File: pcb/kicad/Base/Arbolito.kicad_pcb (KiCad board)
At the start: 2 copper layers, 73 x 66 mm, 61 parts, among them J1 Battery, J2 Conn_01x06_Female, P1 USB_C_Plug_USB2.0, Q1 S8050, Q2 S8050, Q3 S8050, SW1 SW_DP3T, SW2 SW_Push, SW3 SW_Push, SW4 SW_Push, U1 NCP115AMX120TCG, U2 CH340C, U3 AP63205WU, U4 ESP-12F, U5 SHT31-DIS

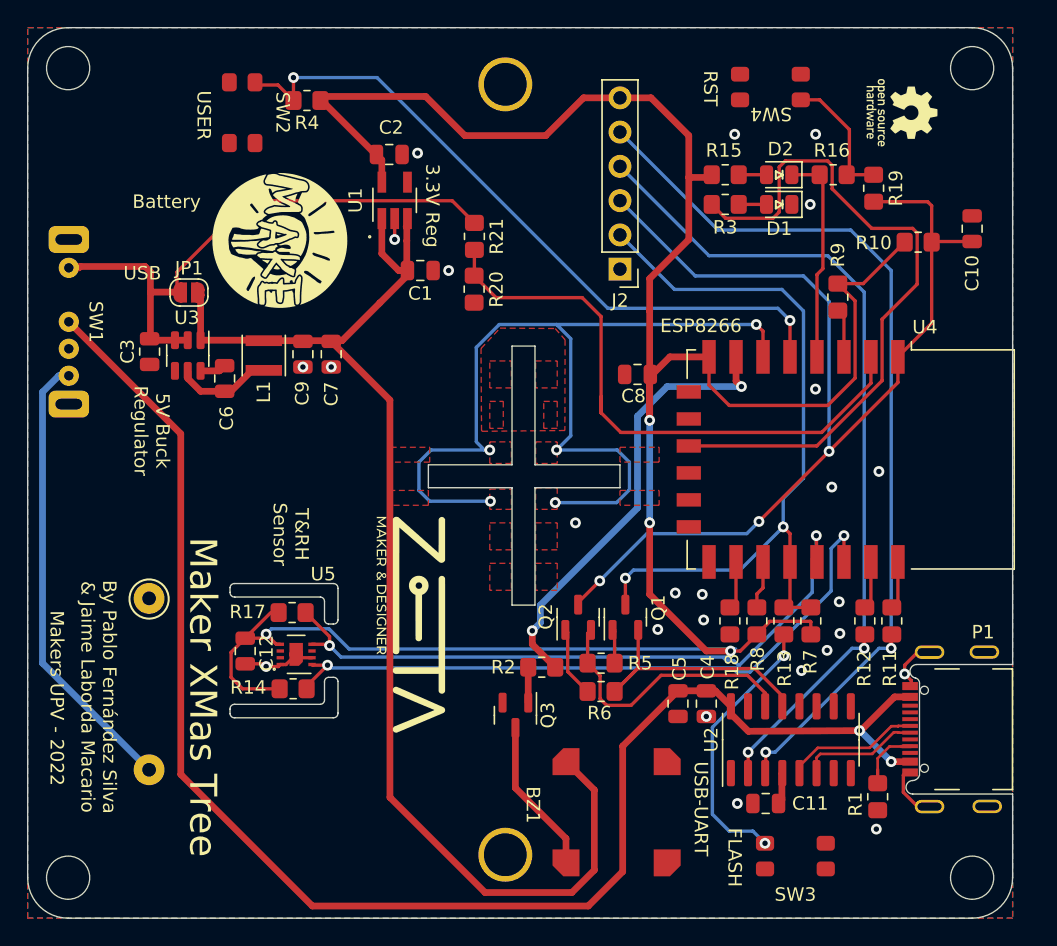
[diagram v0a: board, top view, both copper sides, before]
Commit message: Footprints corrected
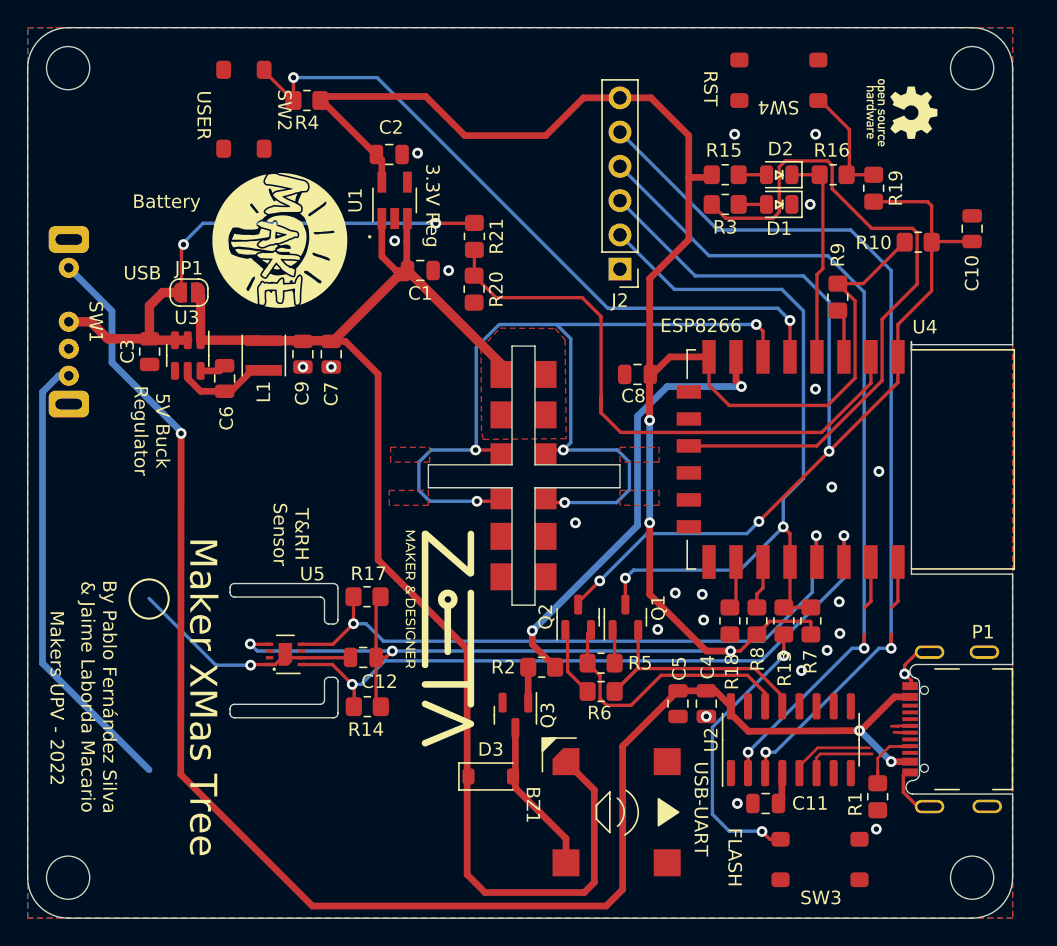
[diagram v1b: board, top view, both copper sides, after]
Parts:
- removed J1: Battery, Library:Battery
- removed R11, R12: 330, Resistor_SMD:R_0805_2012Metric_Pad1.20x1.40mm_HandSolder
- added D3: SD103AW, Diode_SMD:D_SOD-123, F.Cu at (139.3, 117.5)
- added J10: Conn_01x01, Library:Pad_tree_PS, F.Cu at (140.1, 87.7)
- added J11: Conn_01x01, Library:Pad_tree_PS, F.Cu at (140.1, 99.7)
- added J12: Conn_01x01, Library:Pad_tree_PS, F.Cu at (143.4, 102.7)
- added J13: Conn_01x01, Library:Pad_tree_PS, F.Cu at (140.1, 102.7)
- added J14: Conn_01x01, Library:Pad_tree_PS, F.Cu at (143.4, 99.7)
- added J3: Conn_01x01, Library:Pad_tree_Data, F.Cu at (140.1, 93.6)
- added J4: Conn_01x01, Library:Pad_tree_Data, F.Cu at (143.4, 93.6)
- added J5: Conn_01x01, Library:Pad_tree_Data, F.Cu at (143.4, 96.9)
- added J6: Conn_01x01, Library:Pad_tree_Data, F.Cu at (140.1, 96.9)
- added J7: Conn_01x01, Library:Pad_tree_PS, F.Cu at (143.4, 87.7)
- added J8: Conn_01x01, Library:Pad_tree_PS, F.Cu at (140.1, 90.7)
- added J9: Conn_01x01, Library:Pad_tree_PS, F.Cu at (143.4, 90.7)
- moved C12 8.76 mm to (129.9, 108.7), turned to 180 degrees
- moved R17 5.67 mm to (130.2, 104.2), turned to 0 degrees
- moved R14 5.66 mm to (130.2, 112.3), turned to 0 degrees
- moved G*** 2.38 mm to (135.6, 107.3)
- moved SW3 1.92 mm to (163.8, 123.7)
- moved U5 0.80 mm to (124.1, 108.5)
- moved SW4 0.74 mm to (160.6, 65.9)
- moved SW2 0.22 mm to (121.0, 68.1)
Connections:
- net /Boton renamed /BUTTON
- SW1 pad 1: VCC -> VBUS
- SW1 pad 2: VBUS -> VCC
- U4 pad 21: Net-(U4-GPIO3/RXD) -> /TX
- U4 pad 22: Net-(U4-GPIO1/TXD) -> /RX
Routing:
- net +5V: track 91.9 -> 103.7 mm
- net GND: track 13.6 -> 24.0 mm
- net VBUS: track 114.6 -> 119.4 mm, vias 2 -> 3
- net /TX: track 62.8 -> 66.3 mm
- net /RX: track 67.5 -> 71.0 mm
- net Net-(U4-GPIO3/RXD): track 3.56 -> 0.00 mm
- net Net-(U4-GPIO1/TXD): track 3.56 -> 0.00 mm
- net /DIN: track 69.5 -> 72.3 mm
- net /D+: track 8.87 -> 6.61 mm
- net /D-: track 9.44 -> 7.17 mm
- net VCC: track 42.9 -> 40.7 mm, vias 0 -> 2
- net +3.3V: track 176.3 -> 174.8 mm, vias 4 -> 5
- net Net-(R16-Pad1): track 9.94 -> 8.54 mm
- net Net-(R13-Pad1): track 20.5 -> 21.5 mm
- net /SCL: track 49.9 -> 49.0 mm
- removed copper zone on F.Cu, net /DIN
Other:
- outline, holes or cut-outs redrawn

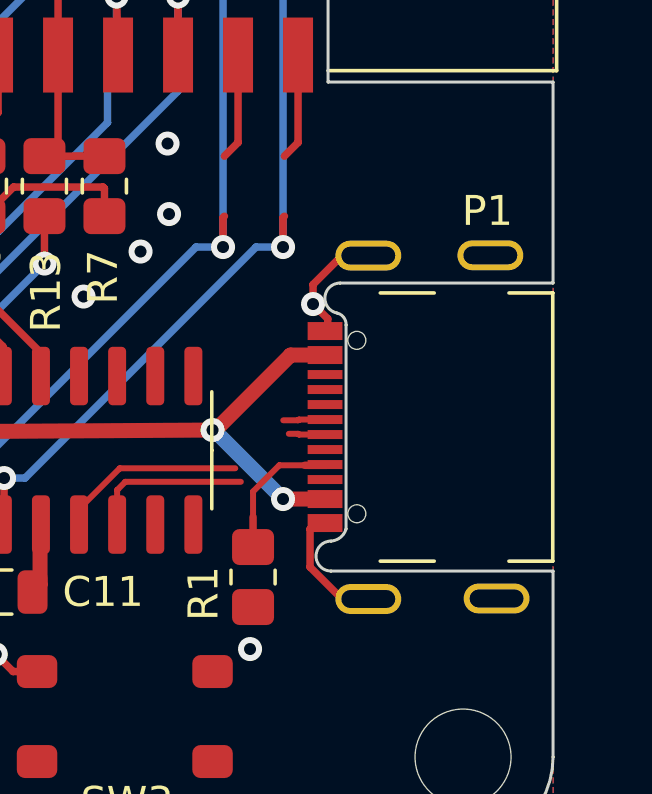
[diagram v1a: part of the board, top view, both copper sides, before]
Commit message: Modified USB C Molex 2169900002 footprint and added 3D step
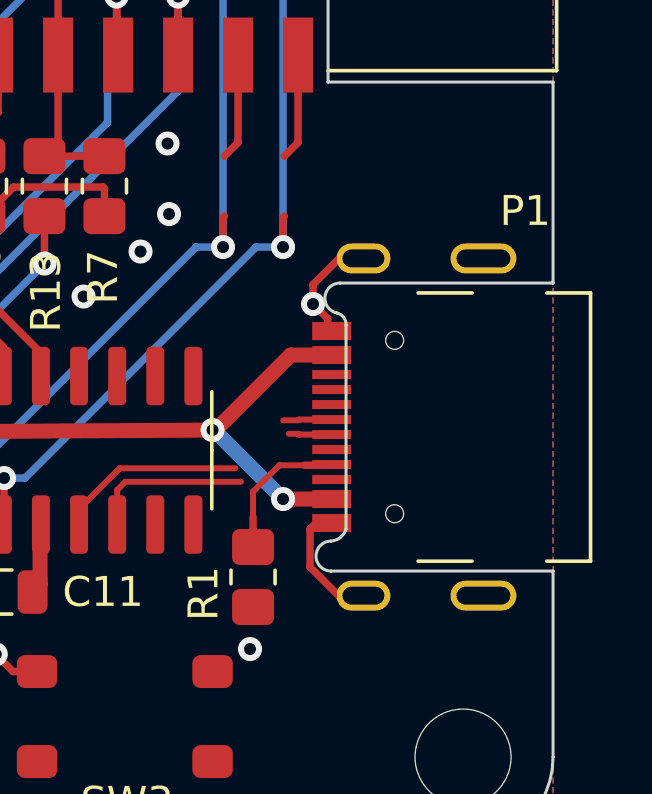
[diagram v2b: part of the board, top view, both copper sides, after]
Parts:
- moved P1 1.26 mm to (174.2, 114.0)

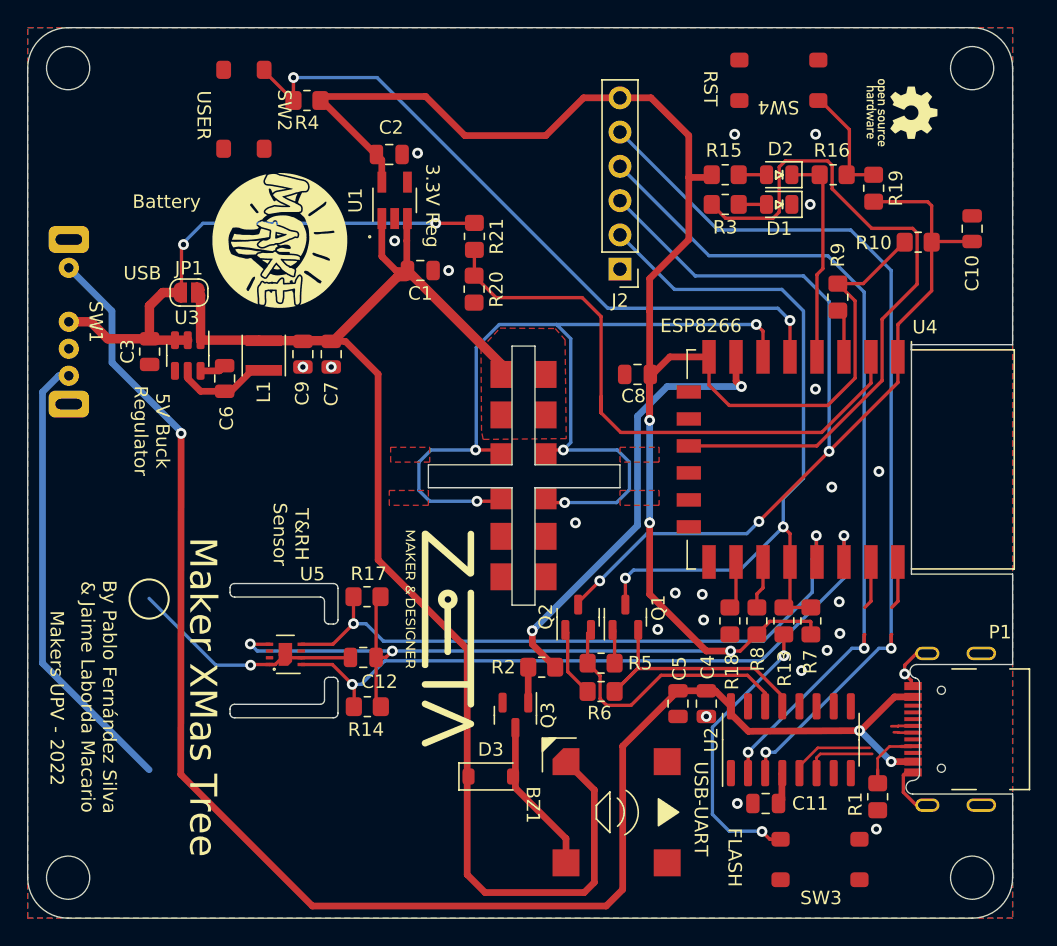
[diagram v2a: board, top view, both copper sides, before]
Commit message: BatteryHolder on place :3
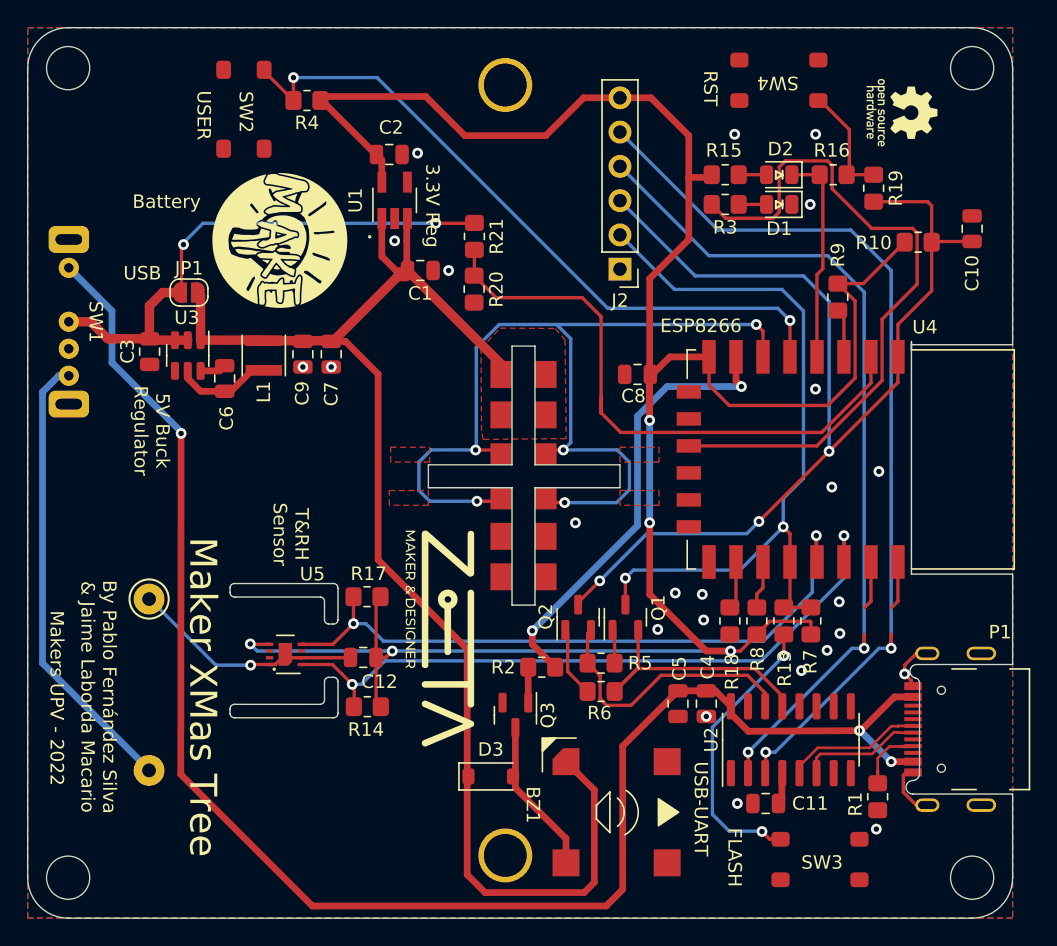
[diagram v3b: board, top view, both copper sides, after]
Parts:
- added J1: Battery, Library:Battery, B.Cu at (140.4, 117.0)
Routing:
- net /D+: track 6.61 -> 8.87 mm
- net /D-: track 7.17 -> 9.44 mm

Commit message: Data lines fixed
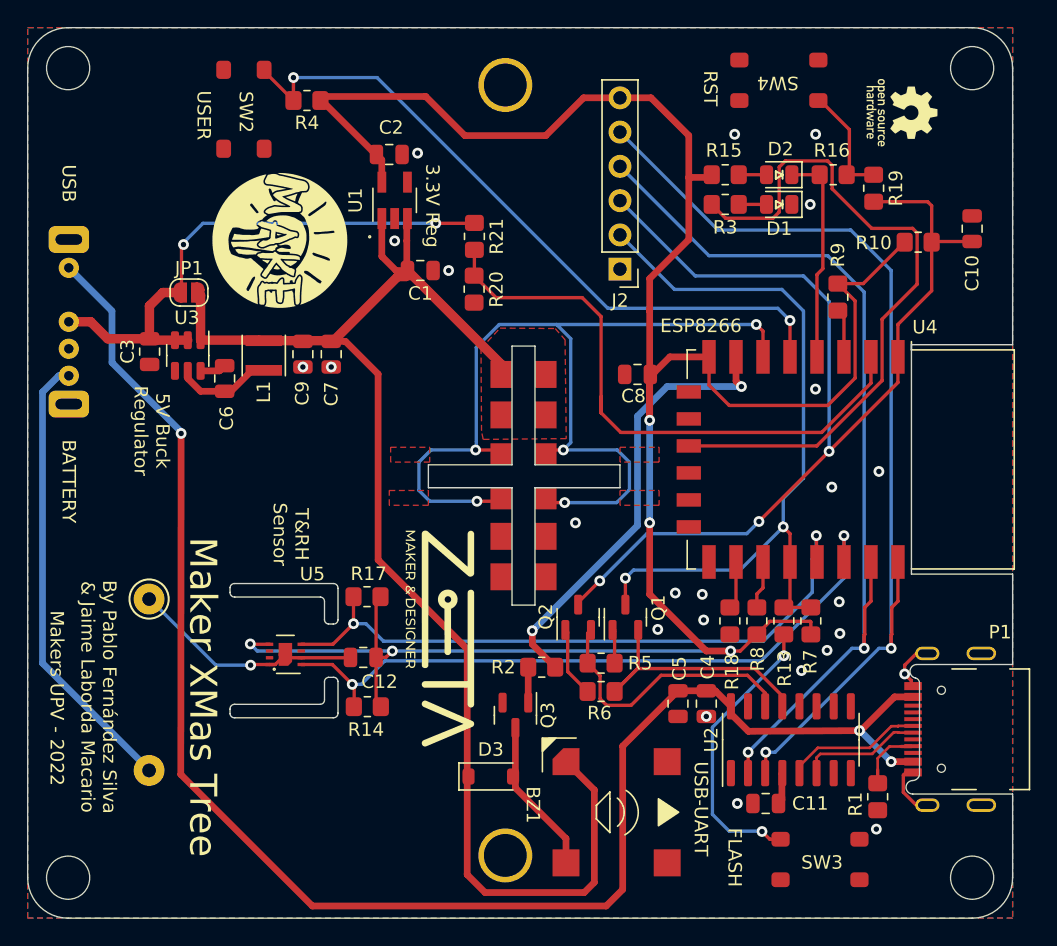
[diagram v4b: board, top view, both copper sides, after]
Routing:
- net /TX: track 66.3 -> 68.3 mm
- net /RX: track 71.0 -> 73.0 mm
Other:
- board text added: "BATTERY"
- board text removed: "Battery"
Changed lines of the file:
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@@
     (property "ki_keywords" "switch dp3t ON-ON-ON")
     (attr smd)
-    (fp_text reference "SW1" (at 0 -3.75 -90 unlocked) (layer "F.SilkS")
+    (fp_text reference "SW1" (at 0.025 -0.125 -90 unlocked) (layer "F.SilkS") hide
         (effects (font (size 1 1) (thickness 0.15)))
     )
@@
     )
   )
-  (footprint "Library:Battery" (layer "B.Cu")
+  (footprint "Library:Battery" locked (layer "B.Cu")
     (at 140.4 117.05 -90)
     (property "Sheetfile" "Arbolito.kicad_sch")
@@
     (fp_rect (start -53.4 -27.79) (end 9 29.21)
       (stroke (width 0.12) (type solid)) (fill none) (layer "B.SilkS"))
-    (pad "1" thru_hole circle (at -12.7 26.4 270) (size 2.286 2.286) (drill 1.02) (layers "*.Cu" "*.Mask")
+    (pad "1" thru_hole circle locked (at -12.7 26.4 270) (size 2.286 2.286) (drill 1.02) (layers "*.Cu" "*.Mask")
       (net 2 "GND") (pinfunction "Pin_1") (pintype "passive"))
-    (pad "2" thru_hole circle (at 0 26.4 270) (size 2.286 2.286) (drill 1.02) (layers "*.Cu" "*.Mask")
+    (pad "2" thru_hole circle locked (at 0 26.4 270) (size 2.286 2.286) (drill 1.02) (layers "*.Cu" "*.Mask")
       (net 22 "Net-(J1-Pin_2)") (pinfunction "Pin_2") (pintype "passive"))
-    (pad "3" thru_hole circle (at -50.8 0 270) (size 4 4) (drill 3.18) (layers "*.Cu" "*.Mask"))
-    (pad "3" thru_hole circle (at 6.3 0 270) (size 4 4) (drill 3.18) (layers "*.Cu" "*.Mask"))
+    (pad "3" thru_hole circle locked (at -50.8 0 270) (size 4 4) (drill 3.18) (layers "*.Cu" "*.Mask"))
+    (pad "3" thru_hole circle locked (at 6.3 0 270) (size 4 4) (drill 3.18) (layers "*.Cu" "*.Mask"))
+    (model "${KIPRJMOD}/Library.pretty/3dmodels/BatteryHolder/keystone-PN2477.STEP"
+      (offset (xyz -21.4 -0.7 7.1))
+      (scale (xyz 1 1 1))
+      (rotate (xyz -90 0 -90))
+    )
   )
   (footprint "LOGO" (layer "B.Cu")
@@
     (effects (font (size 1 1) (thickness 0.15)))
   )
-  (gr_text "Battery" (at 115.3 74.9) (layer "F.SilkS")
+  (gr_text "BATTERY" (at 108.05 95.63 270) (layer "F.SilkS" knockout)
     (effects (font (size 1 1) (thickness 0.15)))
   )
@@
     (effects (font (size 1 1) (thickness 0.15)))
   )
-  (gr_text "USB" (at 113.5 80.2) (layer "F.SilkS")
+  (gr_text "USB" (at 108.05 73.54 270) (layer "F.SilkS" knockout)
     (effects (font (size 1 1) (thickness 0.15)))
   )
@@
   (segment (start 116.4 78.225) (end 116.4 81.54) (width 0.25) (layer "F.Cu") (net 4))
   (segment (start 116.31 81.63) (end 116.28 81.6) (width 0.7) (layer "F.Cu") (net 4))
-  (segment (start 138.08 76.5) (end 138.11 76.47) (width 0.25) (layer "F.Cu") (net 4))
   (segment (start 116.31 81.63) (end 115.02 81.63) (width 0.7) (layer "F.Cu") (net 4))
   (segment (start 114.025 85.045) (end 114.04 85.06) (width 0.7) (layer "F.Cu") (net 4))
@@
   (segment (start 135.275 76.5) (end 135.325 76.55) (width 0.25) (layer "B.Cu") (net 4))
   (segment (start 135.25 76.5) (end 135.275 76.5) (width 0.25) (layer "B.Cu") (net 4))
-  (segment (start 138.11 76.47) (end 138.08 76.5) (width 0.25) (layer "B.Cu") (net 4))
   (segment (start 118 76.5) (end 116.55 77.95) (width 0.25) (layer "B.Cu") (net 4))
   (segment (start 116.55 78.075) (end 116.525 78.075) (width 0.25) (layer "B.Cu") (net 4))
@@
   (segment (start 159.7625 72.9) (end 157.7 72.9) (width 0.25) (layer "F.Cu") (net 15))
   (segment (start 159.7 115.7) (end 159.7 117.21) (width 0.25) (layer "F.Cu") (net 16))
+  (segment (start 169.046 104.97) (end 169.046 106.97) (width 0.25) (layer "F.Cu") (net 16))
   (segment (start 169 107.016) (end 169.046 106.97) (width 0.25) (layer "F.Cu") (net 16))
   (segment (start 169 108) (end 169 107.016) (width 0.25) (layer "F.Cu") (net 16))
@@
   (segment (start 158.4 115.7) (end 158.4 117.24) (width 0.25) (layer "F.Cu") (net 18))
   (segment (start 167.5 104.516) (end 167.046 104.97) (width 0.25) (layer "F.Cu") (net 18))
+  (segment (start 167.046 104.97) (end 167.046 106.97) (width 0.25) (layer "F.Cu") (net 18))
   (segment (start 167 108) (end 167 107.016) (width 0.25) (layer "F.Cu") (net 18))
   (segment (start 167 107.016) (end 167.046 106.97) (width 0.25) (layer "F.Cu") (net 18))

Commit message: Modified USB-C with 3 cents version
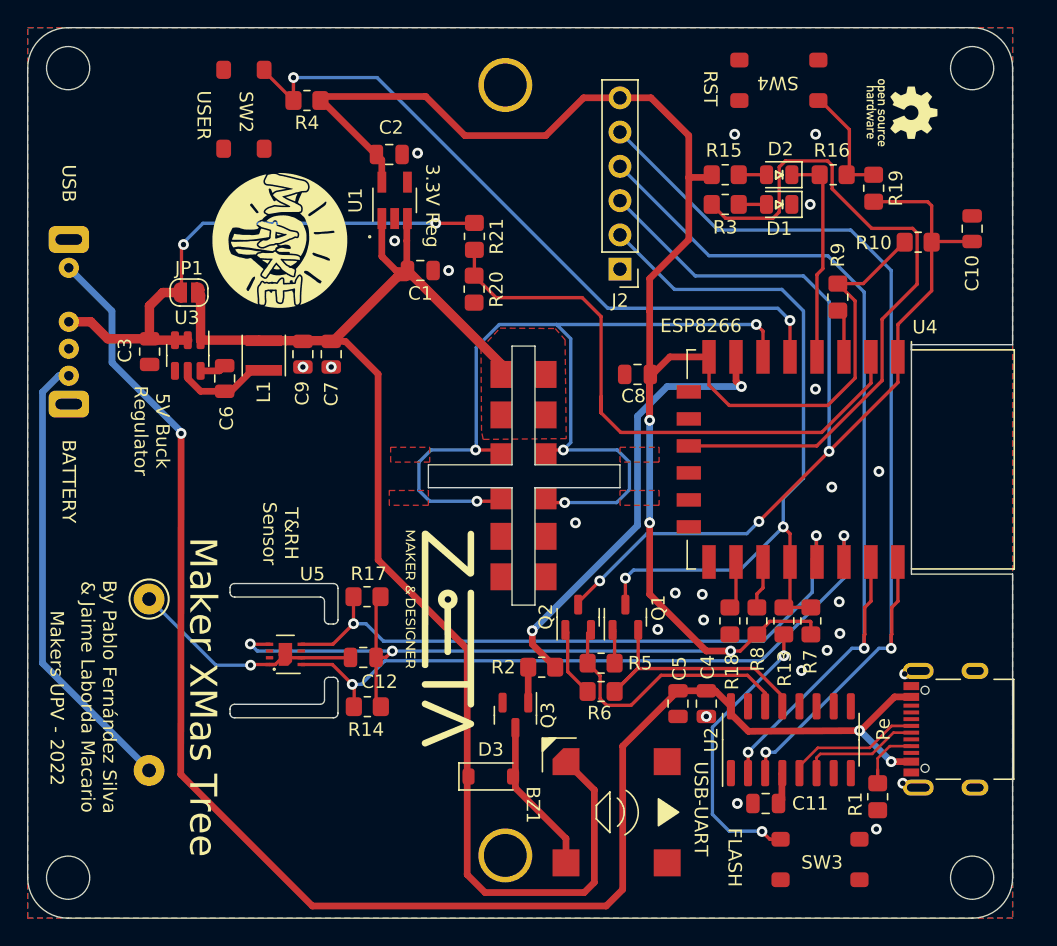
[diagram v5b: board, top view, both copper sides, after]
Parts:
- Pe: renamed from P1; value USB_C_Plug_USB2.0 -> TYPE-C 16PIN 2MD(073); footprint Library:USB C Molex -> Library:TYPE-C 16PIN 2MD(073)
- moved Pe 1.17 mm to (173.0, 114.0)
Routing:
- net GND: track 24.0 -> 17.4 mm, vias 25 -> 26
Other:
- outline, holes or cut-outs redrawn
